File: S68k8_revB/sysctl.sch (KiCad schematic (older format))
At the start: 19 parts, among them U11 74LS393, U12 74LS04, U7 74LS07, U9 ATF16V8C, Y1 16M, Y2 10M

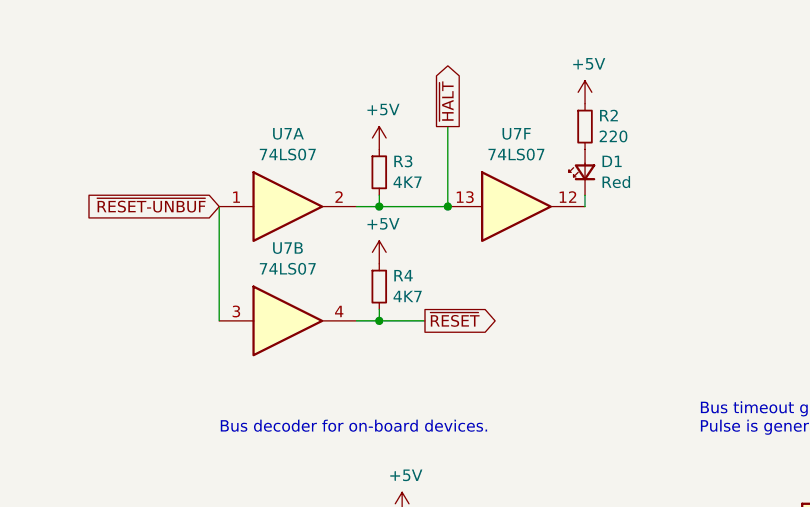
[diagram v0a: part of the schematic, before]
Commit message: S68k8: moved copper pours for power distribution to the bottom layer
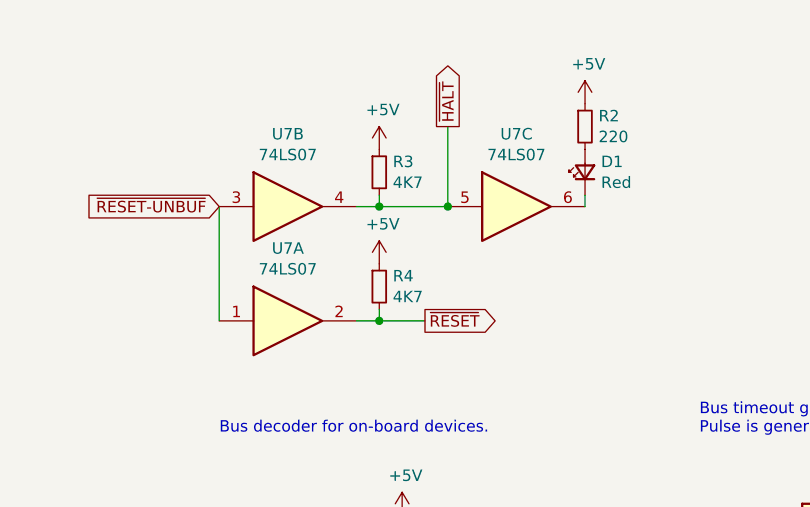
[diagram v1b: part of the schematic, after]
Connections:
- net ~HALT: now also U7.4, U7.5; no longer U7.13, U7.2
- net ~RESET: now also U7.2; no longer U7.4
- net ~RESET-UNBUF: now also U7.1, U7.3; no longer U7.1, U7.3
- net at D1.1 (K): now also U7.6; no longer U7.12
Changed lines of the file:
@@
 $Comp
 L 74xx:74LS07 U7
-U 1 1 605DC63B
+U 2 1 605DC63B
 P 2850 1400
 F 0 "U7" H 2850 1717 50  0000 C CNN
@@
 F 2 "Package_DIP:DIP-14_W7.62mm" H 2850 1400 50  0001 C CNN
 F 3 "www.ti.com/lit/ds/symlink/sn74ls07.pdf" H 2850 1400 50  0001 C CNN
-	1    2850 1400
+	2    2850 1400
 	1    0    0    -1
 $EndComp
 $Comp
 L 74xx:74LS07 U7
-U 2 1 605DD23E
+U 1 1 605DD23E
 P 2850 1900
 F 0 "U7" H 2850 2217 50  0000 C CNN
@@
 F 2 "Package_DIP:DIP-14_W7.62mm" H 2850 1900 50  0001 C CNN
 F 3 "www.ti.com/lit/ds/symlink/sn74ls07.pdf" H 2850 1900 50  0001 C CNN
-	2    2850 1900
+	1    2850 1900
 	1    0    0    -1
 $EndComp
@@
 $Comp
 L 74xx:74LS07 U7
-U 6 1 5FE659BA
+U 3 1 5FE659BA
 P 3850 1400
 F 0 "U7" H 3850 1717 50  0000 C CNN
@@
 F 2 "Package_DIP:DIP-14_W7.62mm" H 3850 1400 50  0001 C CNN
 F 3 "www.ti.com/lit/ds/symlink/sn74ls07.pdf" H 3850 1400 50  0001 C CNN
-	6    3850 1400
-	1    0    0    -1
-$EndComp
+	3    3850 1400
+	1    0    0    -1
+$EndComp
